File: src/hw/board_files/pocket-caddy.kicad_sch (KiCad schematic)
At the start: 0 parts

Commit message: Sch updates
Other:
- added sheet Peripherals (peripherals.kicad_sch)
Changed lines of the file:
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@@
+		)
+	)
+	(sheet
+		(at 176.53 57.15)
+		(size 34.29 52.07)
+		(exclude_from_sim no)
+		(in_bom yes)
+		(on_board yes)
+		(dnp no)
+		(fields_autoplaced yes)
+		(stroke
+			(width 0.1524)
+			(type solid)
+		)
+		(fill
+			(color 0 0 0 0.0000)
+		)
+		(property "Sheetname" "Peripherals"
+			(at 176.53 56.4384 0)
+			(effects
+				(font
+					(size 1.27 1.27)
+				)
+				(justify left bottom)
+			)
+		)
+		(property "Sheetfile" "peripherals.kicad_sch"
+			(at 176.53 109.8046 0)
+			(effects
+				(font
+					(size 1.27 1.27)
+				)
+				(justify left top)
+			)
+		)
+		(instances
+			(project "pocket-caddy"
+				(path "/2c77a8ba-b277-4959-adec-d3fc778c7960"
+					(page "4")
+				)
+			)
 		)
 	)

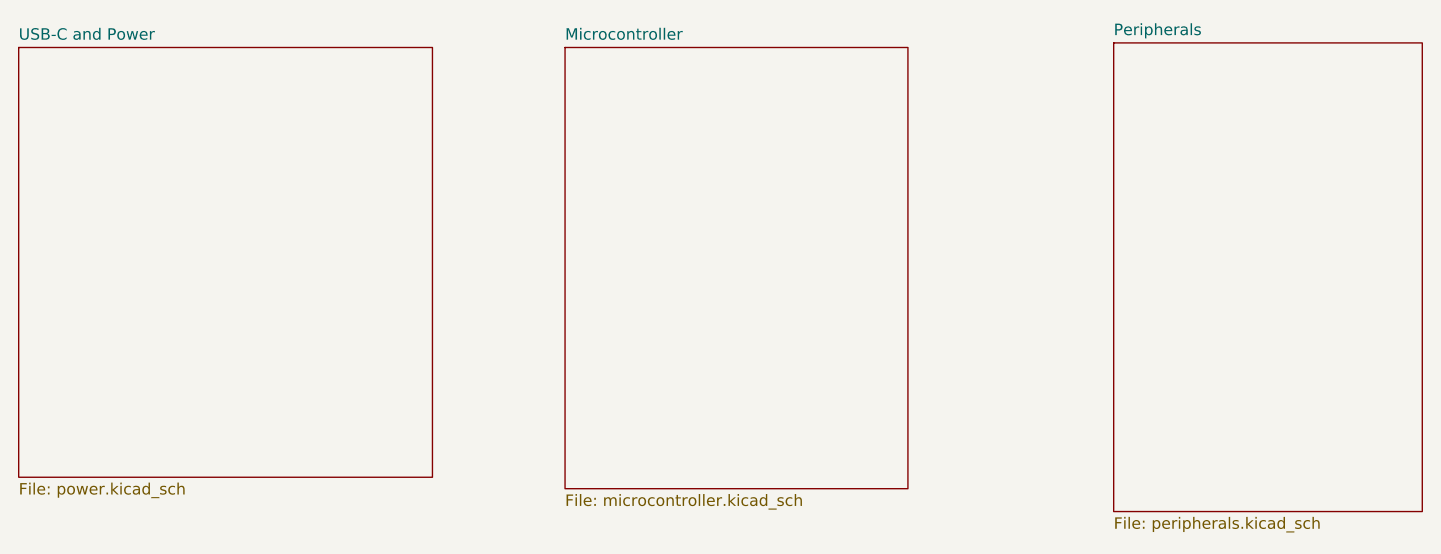
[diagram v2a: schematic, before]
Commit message: Added fuel gauge if, push buttons, jumpers. Need to add test points then review schematic.
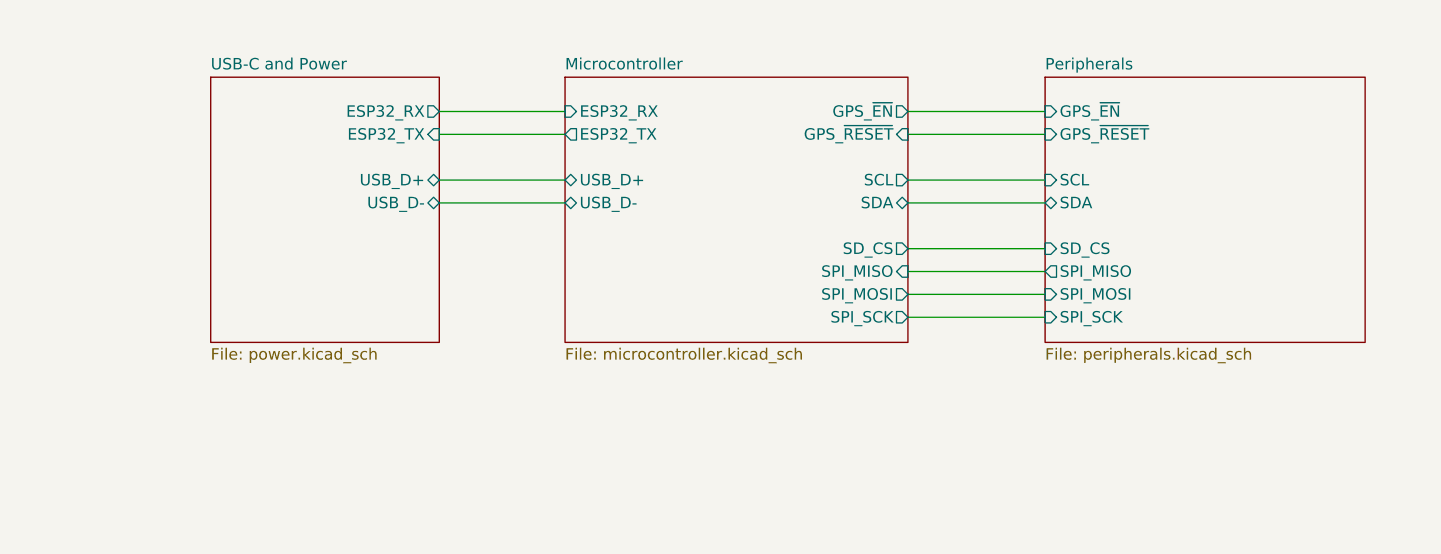
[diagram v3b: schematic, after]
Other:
- sheet Microcontroller ports: added ESP32_RX, ESP32_TX, GPS_~{EN}, GPS_~{RESET}, SCL, SDA, SD_CS, SPI_MISO, SPI_MOSI, SPI_SCK, USB_D+, USB_D-; removed none
- sheet Peripherals ports: added GPS_~{EN}, GPS_~{RESET}, SCL, SDA, SD_CS, SPI_MISO, SPI_MOSI, SPI_SCK; removed none
- sheet USB-C and Power ports: added ESP32_RX, ESP32_TX, USB_D+, USB_D-; removed none

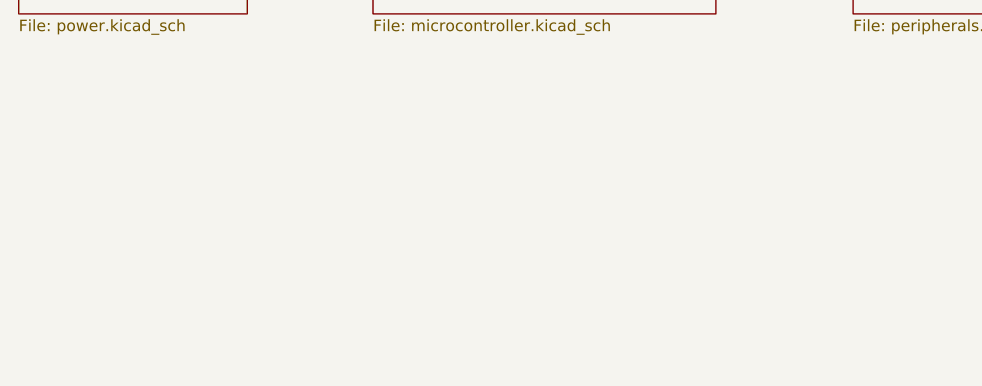
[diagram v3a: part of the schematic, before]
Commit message: Added Test Points to Schematic
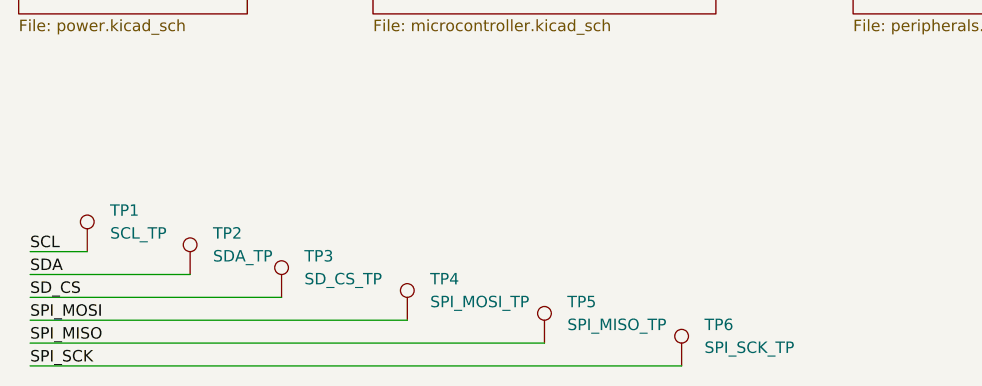
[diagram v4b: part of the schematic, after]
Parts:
- added TP1: SCL_TP, symbol Connector:TestPoint
- added TP2: SDA_TP, symbol Connector:TestPoint
- added TP3: SD_CS_TP, symbol Connector:TestPoint
- added TP4: SPI_MOSI_TP, symbol Connector:TestPoint
- added TP5: SPI_MISO_TP, symbol Connector:TestPoint
- added TP6: SPI_SCK_TP, symbol Connector:TestPoint
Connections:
- new net SCL: TP1.1
- new net SDA: TP2.1
- new net SD_CS: TP3.1
- new net SPI_MISO: TP5.1
- new net SPI_MOSI: TP4.1
- new net SPI_SCK: TP6.1

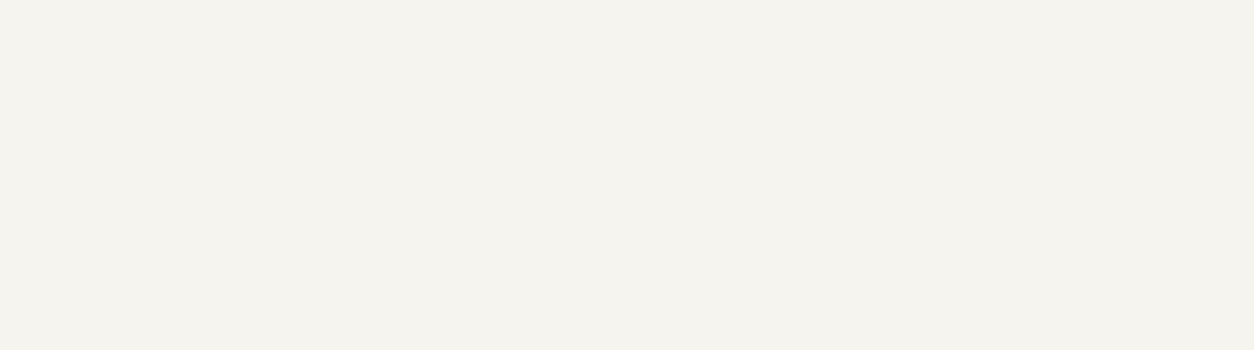
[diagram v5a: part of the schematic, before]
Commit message: Added more footprints and test points
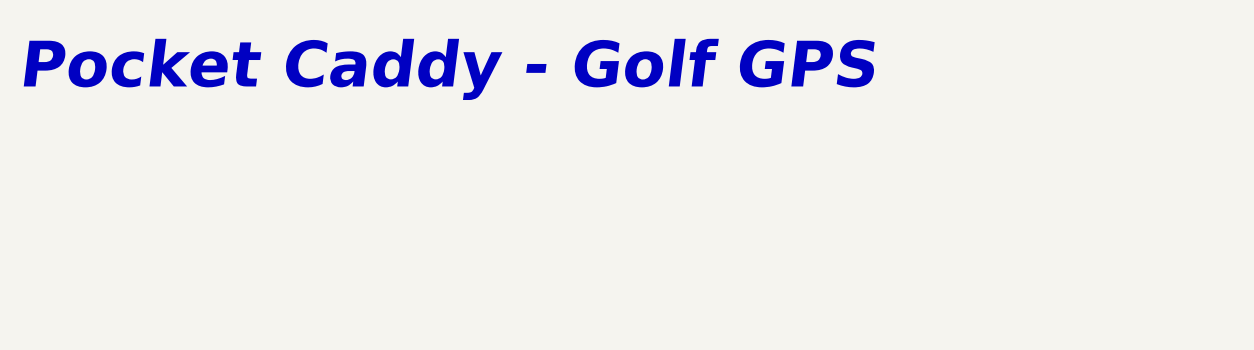
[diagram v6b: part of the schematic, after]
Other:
- note added: "Pocket Caddy - Golf GPS"
- title: Pocket Caddy -> Pocket Caddy - Golf GPS
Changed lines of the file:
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@@
 	(paper "A4")
 	(title_block
-		(title "Pocket Caddy")
-		(date "2025-09-25")
+		(title "Pocket Caddy - Golf GPS")
+		(date "2025-10-03")
 		(rev "0")
 		(company "EE 333 - Electronic Systems Design")
@@
 		(comment 2 "B. York")
 	)
+	(text "Pocket Caddy - Golf GPS"
+		(exclude_from_sim no)
+		(at 14.478 15.748 0)
+		(effects
+			(font
+				(size 5.08 5.08)
+				(thickness 1.016)
+				(bold yes)
+				(italic yes)
+			)
+			(justify left top)
+		)
+	)
 	(wire

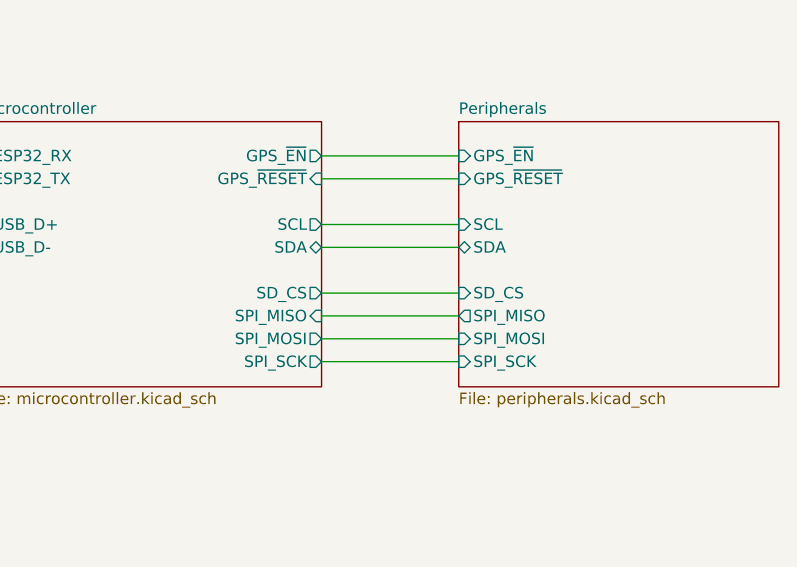
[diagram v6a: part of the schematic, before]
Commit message: Started Layout. Still Need Antenna & LCD Screen added
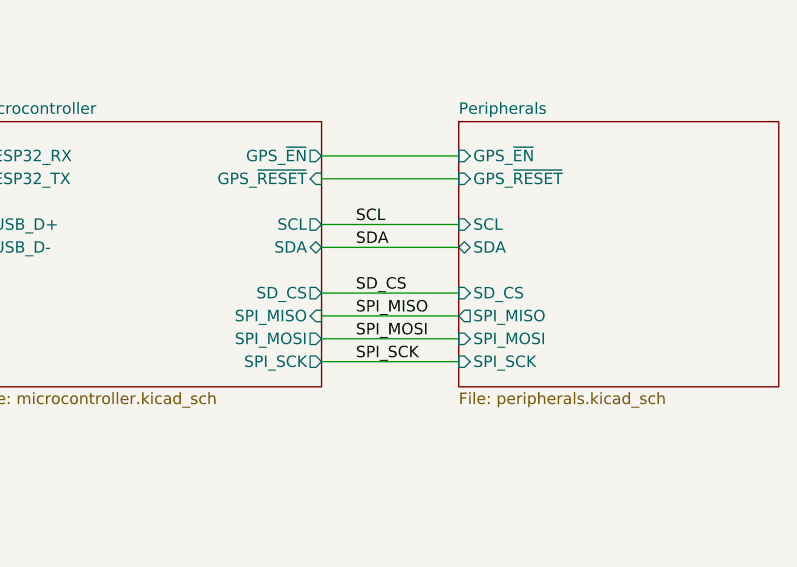
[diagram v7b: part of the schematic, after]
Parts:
- TP1, TP2, TP3, TP4, TP5, TP6: footprint (none) -> TestPoint:TestPoint_Loop_D2.54mm_Drill1.5mm_Beaded
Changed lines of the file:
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@@
+		)
+	)
+	(label "SD_CS"
+		(at 157.48 80.01 0)
+		(effects
+			(font
+				(size 1.27 1.27)
+			)
+			(justify left bottom)
+		)
+	)
+	(label "SCL"
+		(at 157.48 72.39 0)
+		(effects
+			(font
+				(size 1.27 1.27)
+			)
+			(justify left bottom)
 		)
 	)
@@
 		)
 	)
+	(label "SDA"
+		(at 157.48 74.93 0)
+		(effects
+			(font
+				(size 1.27 1.27)
+			)
+			(justify left bottom)
+		)
+	)
 	(label "SD_CS"
 		(at 77.47 121.92 0)
@@
 		)
 	)
+	(label "SPI_MOSI"
+		(at 157.48 85.09 0)
+		(effects
+			(font
+				(size 1.27 1.27)
+			)
+			(justify left bottom)
+		)
+	)
 	(label "SPI_MISO"
 		(at 77.47 127 0)
@@
 		)
 	)
+	(label "SPI_MISO"
+		(at 157.48 82.55 0)
+		(effects
+			(font
+				(size 1.27 1.27)
+			)
+			(justify left bottom)
+		)
+	)
+	(label "SPI_SCK"
+		(at 157.48 87.63 0)
+		(effects
+			(font
+				(size 1.27 1.27)
+			)
+			(justify left bottom)
+		)
+	)
 	(symbol
 		(lib_id "Connector:TestPoint")
@@
 			)
 		)
-		(property "Footprint" ""
+		(property "Footprint" "TestPoint:TestPoint_Loop_D2.54mm_Drill1.5mm_Beaded"
 			(at 139.7 127 0)
 			(effects
@@
 			)
 		)
-		(property "Footprint" ""
+		(property "Footprint" "TestPoint:TestPoint_Loop_D2.54mm_Drill1.5mm_Beaded"
 			(at 154.94 129.54 0)
 			(effects
@@
 			)
 		)
-		(property "Footprint" ""
+		(property "Footprint" "TestPoint:TestPoint_Loop_D2.54mm_Drill1.5mm_Beaded"
 			(at 124.46 124.46 0)
 			(effects
@@
 			)
 		)
-		(property "Footprint" ""
+		(property "Footprint" "TestPoint:TestPoint_Loop_D2.54mm_Drill1.5mm_Beaded"
 			(at 100.33 119.38 0)
 			(effects
@@
 			)
 		)
-		(property "Footprint" ""
+		(property "Footprint" "TestPoint:TestPoint_Loop_D2.54mm_Drill1.5mm_Beaded"
 			(at 110.49 121.92 0)
 			(effects
@@
 			)
 		)
-		(property "Footprint" ""
+		(property "Footprint" "TestPoint:TestPoint_Loop_D2.54mm_Drill1.5mm_Beaded"
 			(at 88.9 116.84 0)
 			(effects

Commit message: Layout progress. Made new footprint for inductor. Changed test  points to pads
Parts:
- TP1, TP2, TP3, TP4, TP5, TP6: footprint TestPoint:TestPoint_Loop_D2.54mm_Drill1.5mm_Beaded -> TestPoint:TestPoint_Pad_D1.5mm; now left out of the parts list
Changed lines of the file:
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@@
 		(unit 1)
 		(exclude_from_sim no)
-		(in_bom yes)
+		(in_bom no)
 		(on_board yes)
 		(dnp no)
@@
 			)
 		)
-		(property "Footprint" "TestPoint:TestPoint_Loop_D2.54mm_Drill1.5mm_Beaded"
+		(property "Footprint" "TestPoint:TestPoint_Pad_D1.5mm"
 			(at 139.7 127 0)
 			(effects
@@
 		(unit 1)
 		(exclude_from_sim no)
-		(in_bom yes)
+		(in_bom no)
 		(on_board yes)
 		(dnp no)
@@
 			)
 		)
-		(property "Footprint" "TestPoint:TestPoint_Loop_D2.54mm_Drill1.5mm_Beaded"
+		(property "Footprint" "TestPoint:TestPoint_Pad_D1.5mm"
 			(at 154.94 129.54 0)
 			(effects
@@
 		(unit 1)
 		(exclude_from_sim no)
-		(in_bom yes)
+		(in_bom no)
 		(on_board yes)
 		(dnp no)
@@
 			)
 		)
-		(property "Footprint" "TestPoint:TestPoint_Loop_D2.54mm_Drill1.5mm_Beaded"
+		(property "Footprint" "TestPoint:TestPoint_Pad_D1.5mm"
 			(at 124.46 124.46 0)
 			(effects
@@
 		(unit 1)
 		(exclude_from_sim no)
-		(in_bom yes)
+		(in_bom no)
 		(on_board yes)
 		(dnp no)
@@
 			)
 		)
-		(property "Footprint" "TestPoint:TestPoint_Loop_D2.54mm_Drill1.5mm_Beaded"
+		(property "Footprint" "TestPoint:TestPoint_Pad_D1.5mm"
 			(at 100.33 119.38 0)
 			(effects
@@
 		(unit 1)
 		(exclude_from_sim no)
-		(in_bom yes)
+		(in_bom no)
 		(on_board yes)
 		(dnp no)
@@
 			)
 		)
-		(property "Footprint" "TestPoint:TestPoint_Loop_D2.54mm_Drill1.5mm_Beaded"
+		(property "Footprint" "TestPoint:TestPoint_Pad_D1.5mm"
 			(at 110.49 121.92 0)
 			(effects
@@
 		(unit 1)
 		(exclude_from_sim no)
-		(in_bom yes)
+		(in_bom no)
 		(on_board yes)
 		(dnp no)
@@
 			)
 		)
-		(property "Footprint" "TestPoint:TestPoint_Loop_D2.54mm_Drill1.5mm_Beaded"
+		(property "Footprint" "TestPoint:TestPoint_Pad_D1.5mm"
 			(at 88.9 116.84 0)
 			(effects
